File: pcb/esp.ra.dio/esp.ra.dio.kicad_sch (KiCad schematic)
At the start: 33 parts, among them J1 A, J10 UART, J2 B, J3 C, J4 D, J5 START, J6 SELECT, J7 JOY, J8 USB_B_Micro, J9 BATTERY, Q1 BSS138, SW1 POWER, SW2 RESET, SW3 BOOT, U2 VCC, U3 RT9080-33GJ5

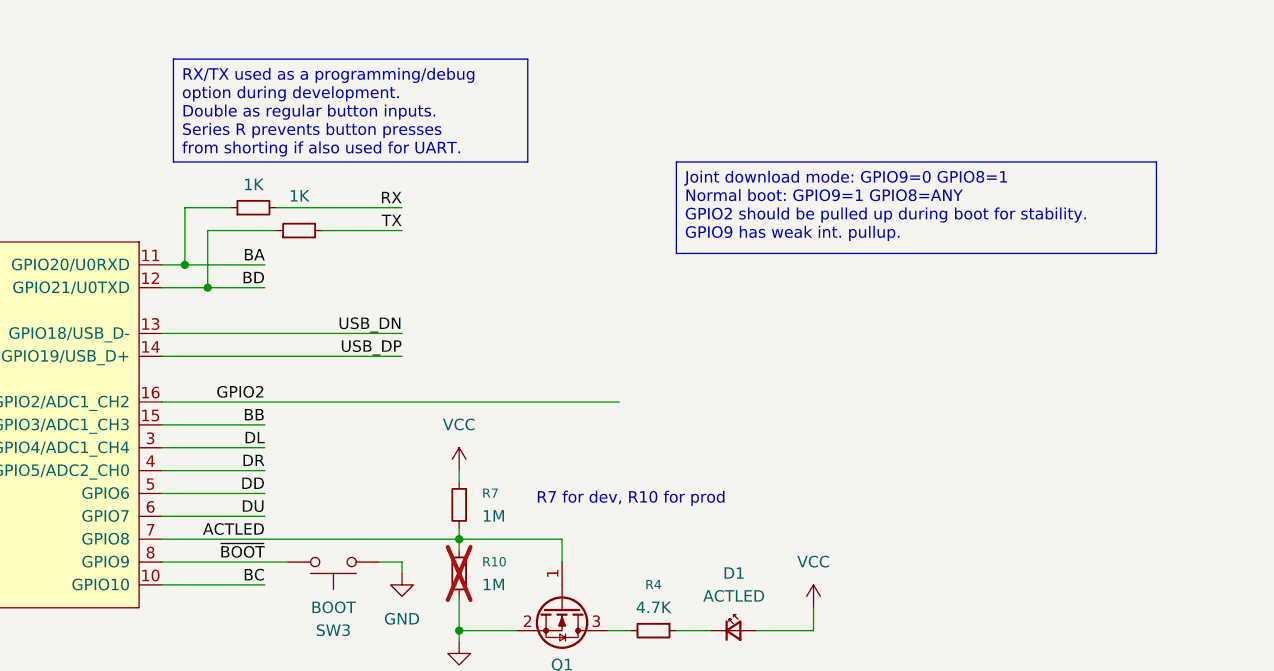
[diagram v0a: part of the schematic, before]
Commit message: Schematic: Bat sense
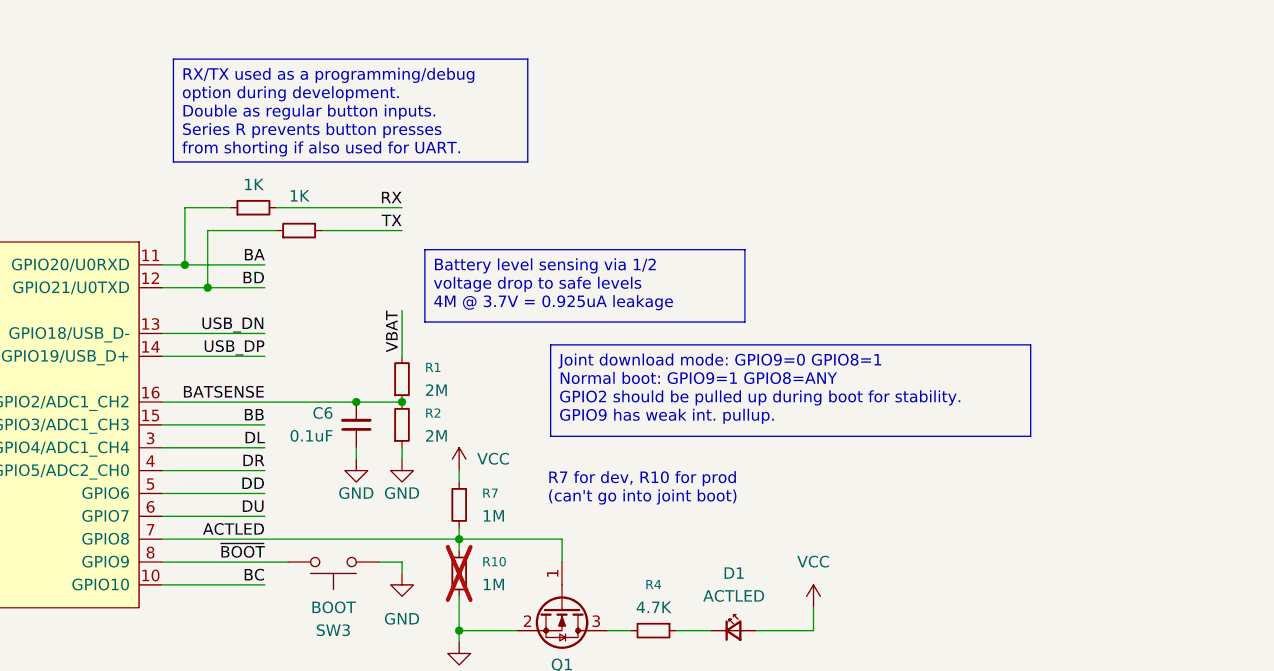
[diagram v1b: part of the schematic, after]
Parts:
- added C6: 0.1uF, symbol Device:C_Small
- added R1, R2: 2M, symbol Device:R_Small
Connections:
- net GND: now also C6.1, R2.1
- net VBAT: now also R1.2
- net GPIO2 renamed BATSENSE
- net BATSENSE: now also C6.2, R1.1, R2.2

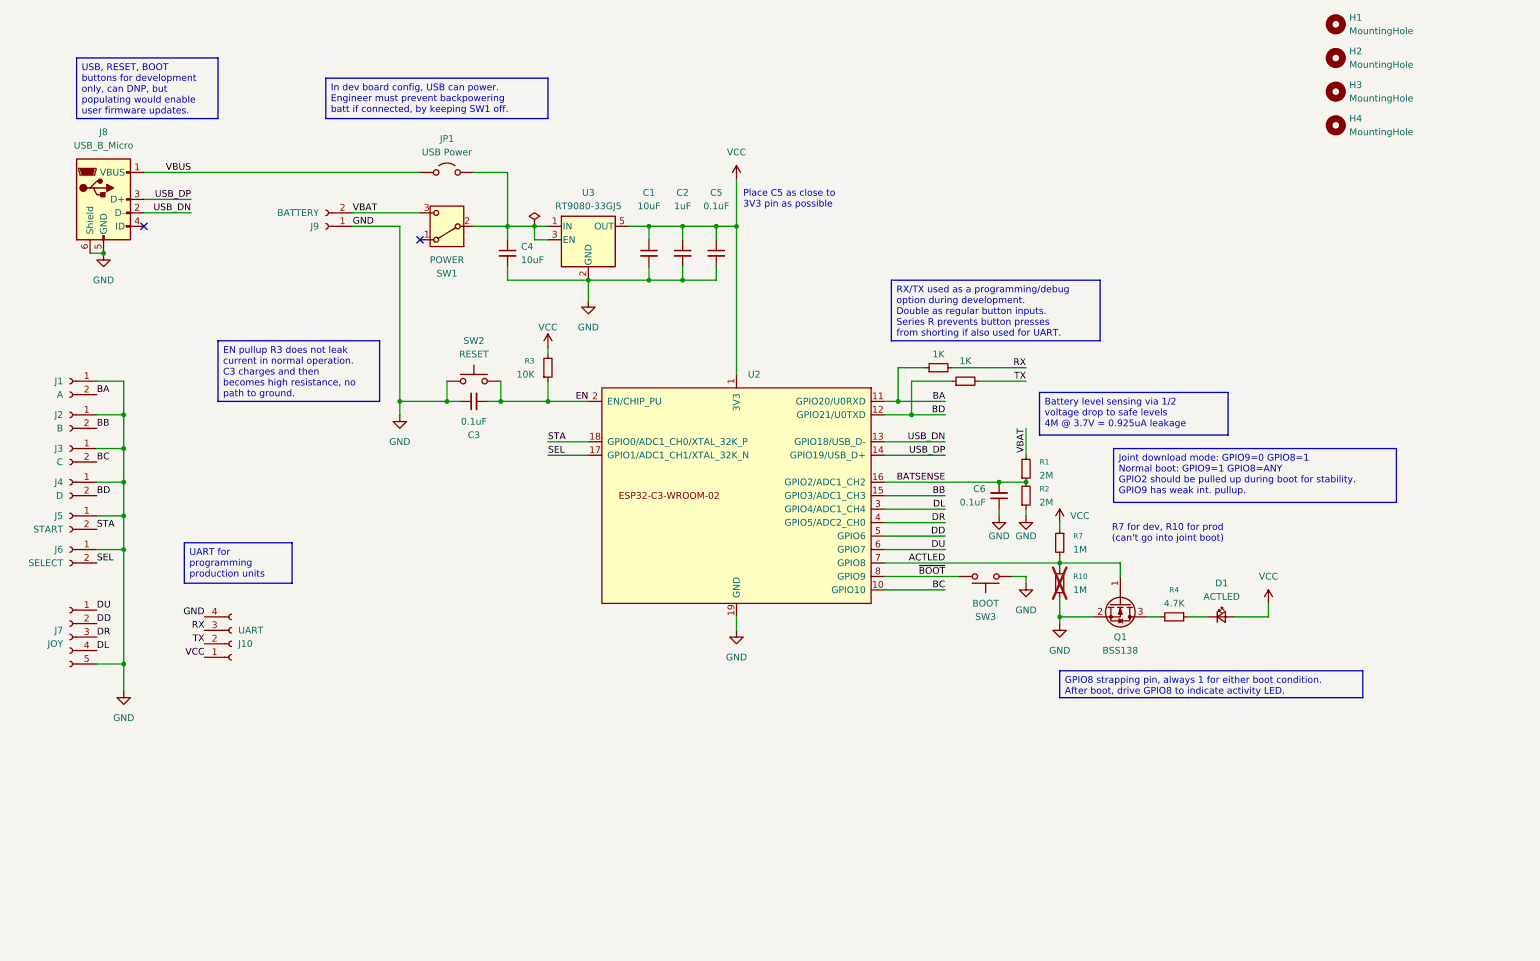
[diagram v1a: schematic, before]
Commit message: WIP converting PCB to use shift register
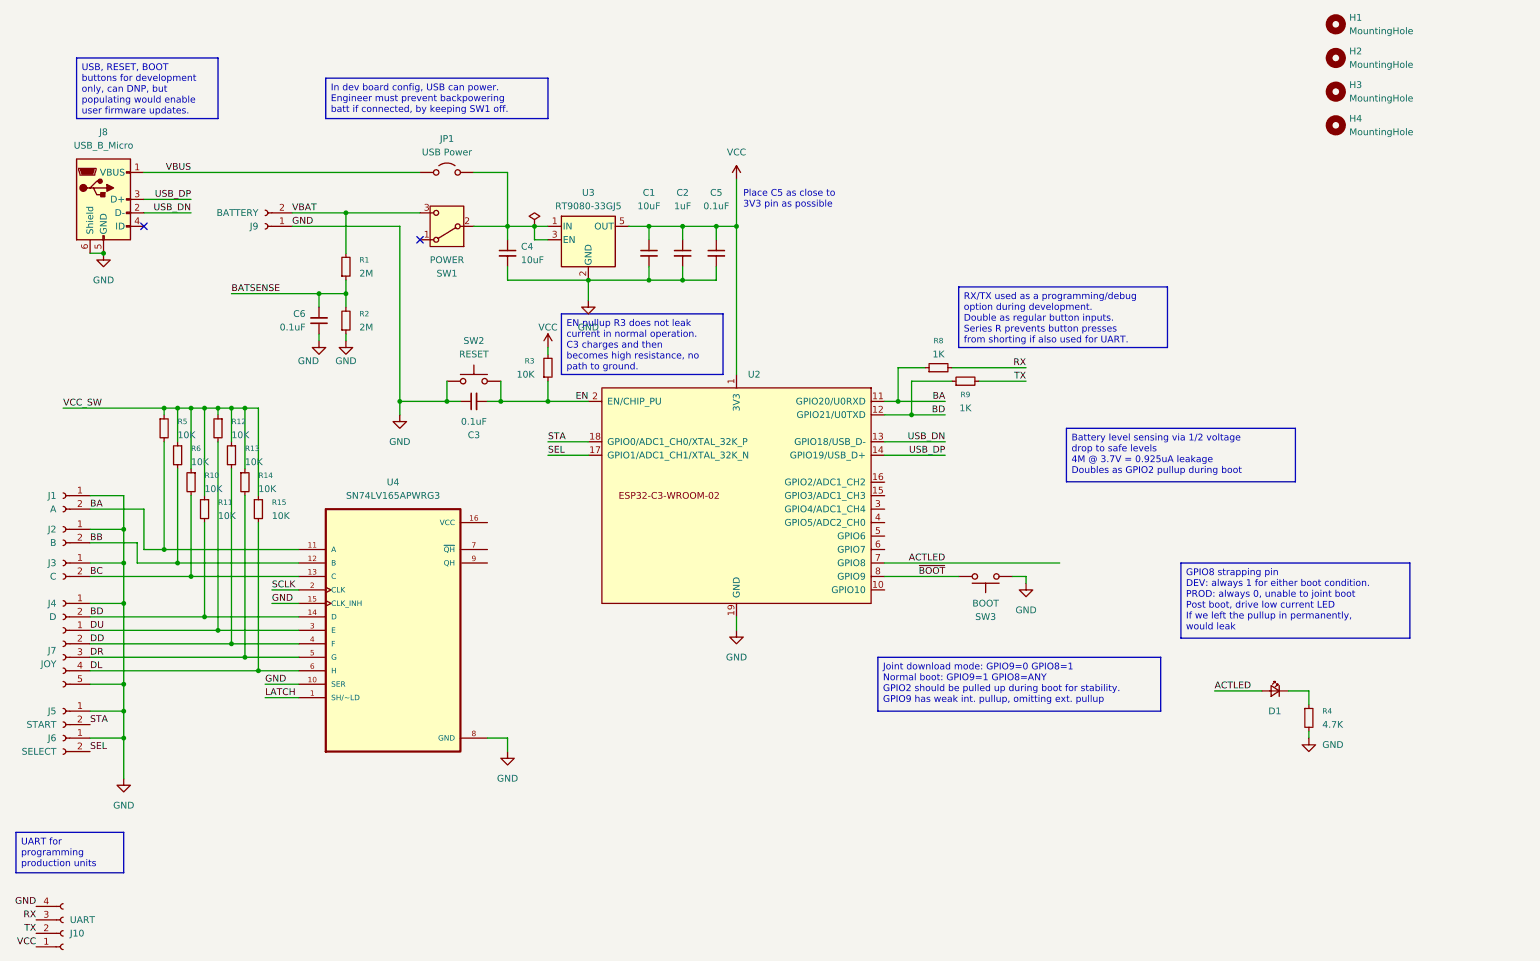
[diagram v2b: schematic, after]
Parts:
- removed Q1: BSS138, Package_TO_SOT_SMD:SOT-23, symbol Transistor_FET:BSS138
- removed R7: 1M, Resistor_SMD:R_0805_2012Metric_Pad1.20x1.40mm_HandSolder, symbol Device:R_Small
- added R11, R12, R13, R14, R15, R5, R6: 10K, symbol Device:R_Small
- added U4: SN74LV165APWRG3, SN74LV165APWRG3:SOP65P640X120-16N, symbol SN74LV165APWRG3:SN74LV165APWRG3
- R10: value 1M -> 10K; footprint Resistor_SMD:R_0805_2012Metric_Pad1.20x1.40mm_HandSolder -> (none); now fitted
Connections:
- net ACTLED: now also D1.2 (A); no longer R10.1
- net BA: now also R5.2, U4.11 (A)
- net BATSENSE: no longer U2.16 (GPIO2/ADC1_CH2)
- net BB: now also R6.2, U4.12 (B); no longer U2.15 (GPIO3/ADC1_CH3)
- net BC: now also R10.2, U4.13 (C); no longer U2.10 (GPIO10)
- net BD: now also R11.2, U4.14 (D)
- net DD: now also R13.2, U4.4 (F); no longer U2.5 (GPIO6)
- net DL: now also R15.2, U4.6 (H); no longer U2.3 (GPIO4/ADC1_CH4)
- net DR: now also R14.2, U4.5 (G); no longer U2.4 (GPIO5/ADC2_CH0)
- net DU: now also R12.2, U4.3 (E); no longer U2.6 (GPIO7)
- net GND: now also R4.2, U4.10 (SER), U4.15 (CLK_INH), U4.8 (GND); no longer R10.2
- net VCC: no longer D1.2 (A)
- new net LATCH: U4.1 (SH/~LD)
- new net SCLK: U4.2 (CLK)
- new net VCC_SW: R10.1, R11.1, R12.1, R13.1, R14.1, R15.1, R5.1, R6.1
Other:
- moved on the sheet: J1, J10, J2, J3, J4, J7, J9

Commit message: Rev4 PCB migrating to shift register, needs new layout
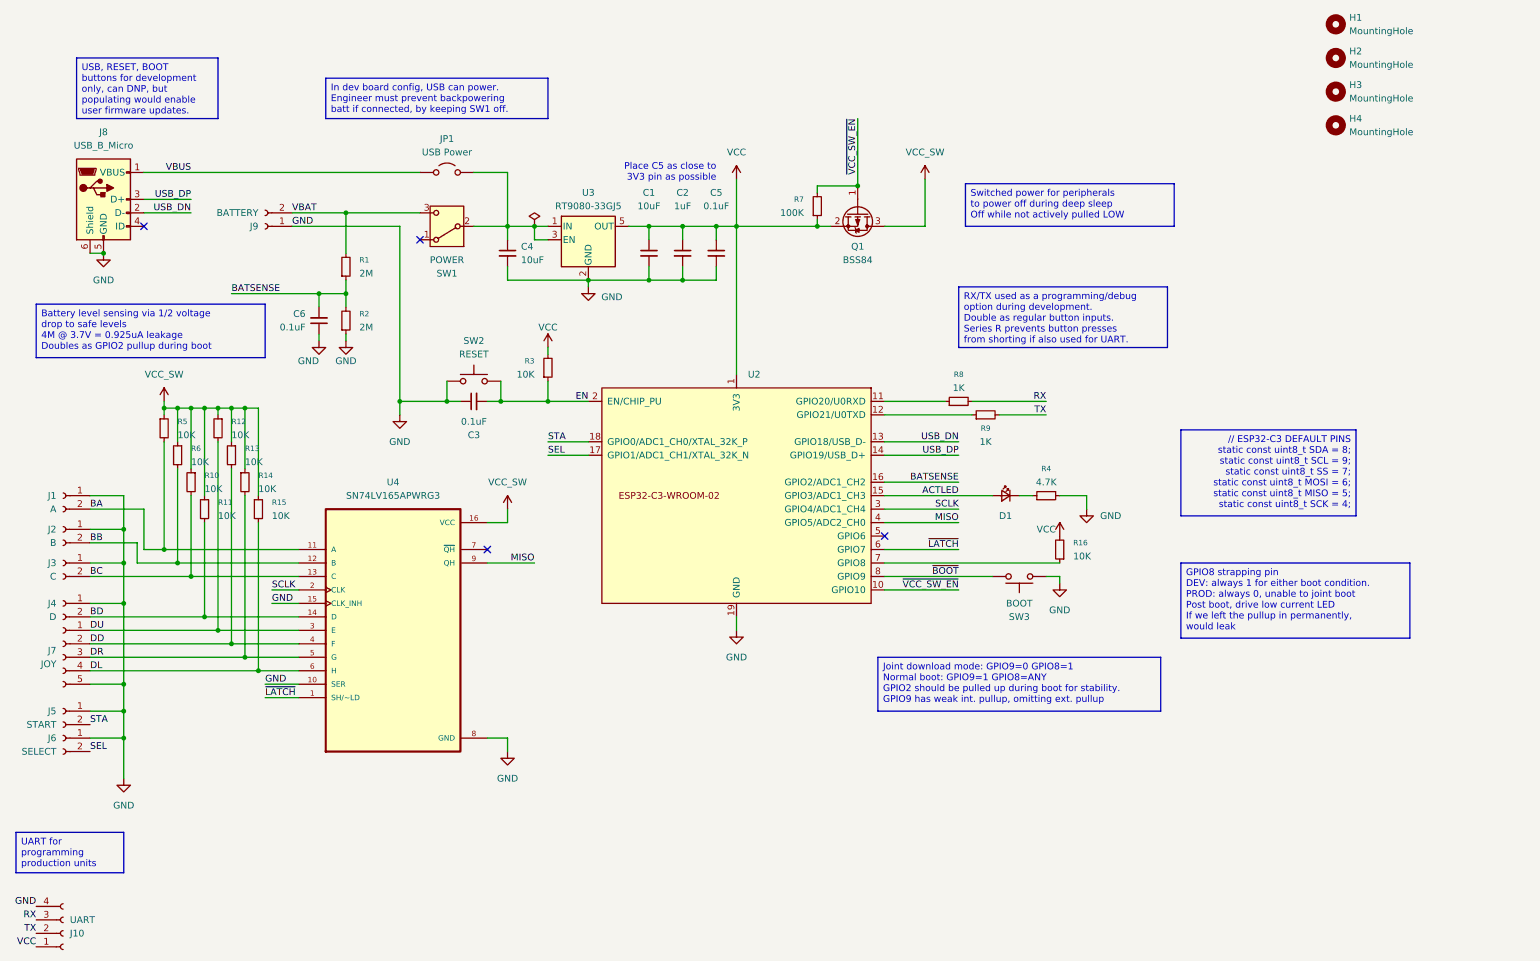
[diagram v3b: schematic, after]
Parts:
- added Q1: BSS84, Package_TO_SOT_SMD:SOT-23, symbol Transistor_FET:BSS84
- added R16: 10K, Resistor_SMD:R_0805_2012Metric_Pad1.20x1.40mm_HandSolder, symbol Device:R_Small
- added R7: 100K, Resistor_SMD:R_0805_2012Metric_Pad1.20x1.40mm_HandSolder, symbol Device:R_Small
- C6: footprint (none) -> Capacitor_SMD:C_0805_2012Metric_Pad1.18x1.45mm_HandSolder
- R1, R10, R11, R12, R13, R14, R15, R2, R5, R6: footprint (none) -> Resistor_SMD:R_0805_2012Metric_Pad1.20x1.40mm_HandSolder
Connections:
- net LATCH is gone; now on net ~{LATCH}: U4.1 (SH/~LD)
- net ACTLED: now also U2.15 (GPIO3/ADC1_CH3); no longer U2.7 (GPIO8)
- net BA: no longer R8.1, U2.11 (GPIO20/U0RXD)
- net BATSENSE: now also U2.16 (GPIO2/ADC1_CH2)
- net BD: no longer R9.1, U2.12 (GPIO21/U0TXD)
- net SCLK: now also U2.3 (GPIO4/ADC1_CH4)
- net VCC: now also Q1.2 (S), R16.2, R7.1
- net VCC_SW: now also U4.16 (VCC), Q1.3 (D)
- net ~{VCC_SW_EN}: now reaches U2.10 (GPIO10)
- net ~{VCC_SW_EN}: now also Q1.1 (G), R7.2
- net MISO: now reaches U2.4 (GPIO5/ADC2_CH0)
- net MISO: now also U4.9 (QH)
- net ~{LATCH}: now reaches U2.6 (GPIO7)
- new net: R8.1, U2.11 (GPIO20/U0RXD)
- new net: R9.1, U2.12 (GPIO21/U0TXD)
- new net: R16.1, U2.7 (GPIO8)
- no-connect marks 2 -> 4
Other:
- moved on the sheet: D1, R4, R8, R9, SW3
